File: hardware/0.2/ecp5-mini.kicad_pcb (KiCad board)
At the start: 4 copper layers, 52 x 27 mm, 105 parts, among them J1 Micro_SD_Card, J2 JTAG, J3 S7 Mini, J4 S7 Mini, J5 USB_C_Receptacle_USB2.0, Q1 BSS138, Q2 BSS138, Q3 BSS138, Q4 BSS138, SW1 PTS810, U1 ECP5U_12_CABGA256, U2 TLV75525PDQNR, U3 TLV75518PDQNR, U4 USBLC6-2P6, U5 TLV62569DRLR, U6 W25Q128JVPIQ, U7 S27KS0641, U8 TLV62569DRLR, X1 DSC6101CI2A-016.0000

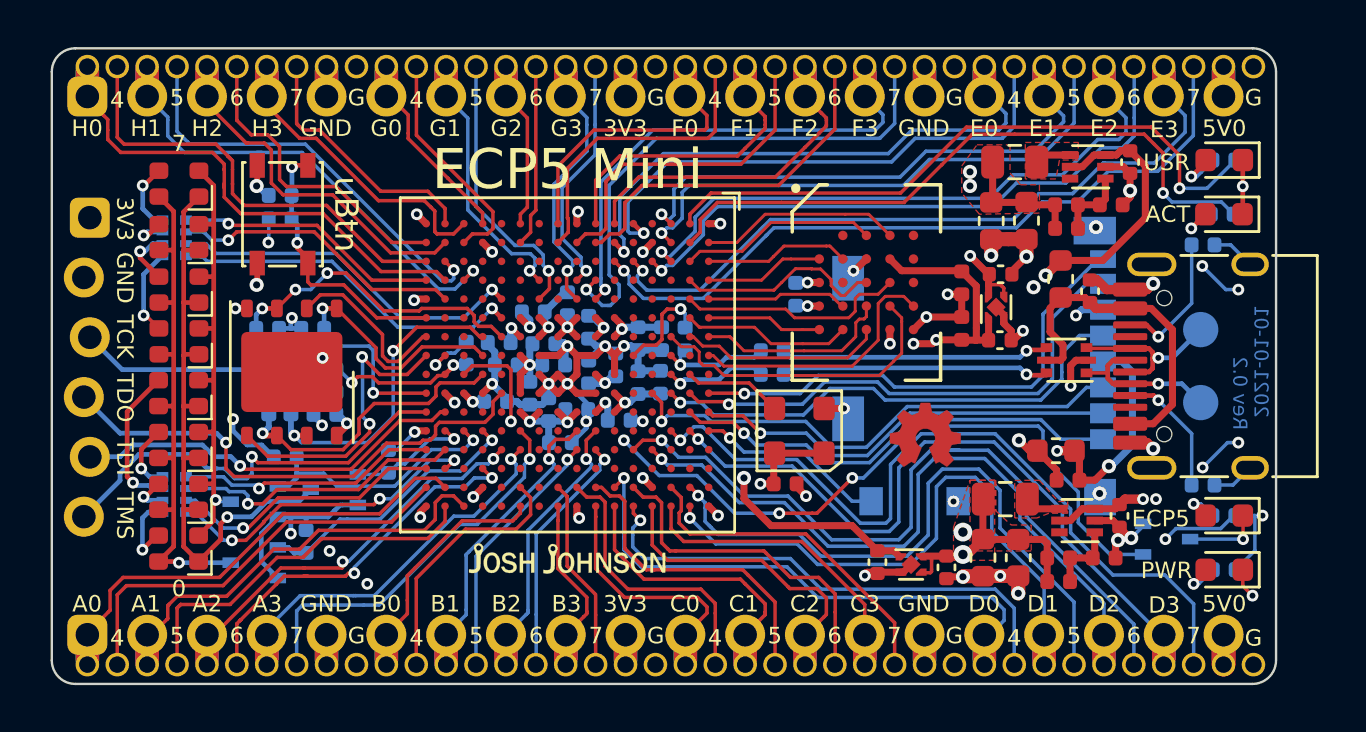
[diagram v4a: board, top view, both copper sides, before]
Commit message: hyperram now length matched
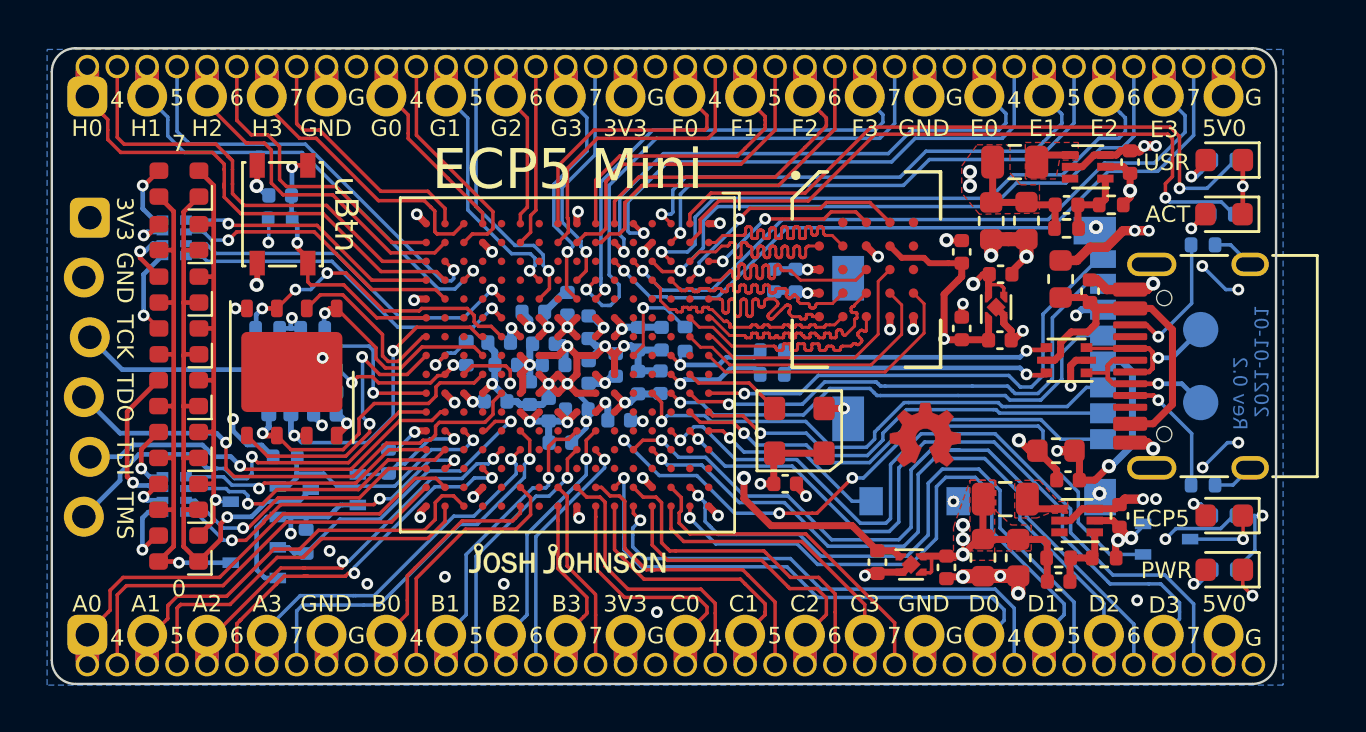
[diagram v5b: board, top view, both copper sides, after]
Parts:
- added C28: 4u7, Capacitor_SMD:C_0402_1005Metric, B.Cu at (126.9, 91.3)
- moved C46 1.32 mm to (134.8, 90.1), turned to 90 degrees
- moved C45 0.59 mm to (127.8, 91.3)
- moved U7 0.55 mm to (130.8, 90.8)
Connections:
- net /FPGA Config/D+ renamed Net-(R10-Pad2)
- net /FPGA Config/D- renamed Net-(R9-Pad1)
- U1 pad A2: /HR_nRST -> /HR_CK_P
- U1 pad A3: /HR_CK -> /HR_nCS
- U1 pad A4: /HR_nCK -> /HR_RWDS
- U1 pad A5: /HR_DQ1 -> /HR_DQ7
- U1 pad A6: /HR_DQ7 -> /HR_DQ0
- U1 pad A7: /HR_DQ0 -> /HR_DQ2
- U1 pad B3: /HR_nCS -> /HR_CK_N
- U1 pad B4: /HR_RWDS -> /HR_nRST
- U1 pad B5: /HR_DQ2 -> (no net)
- U1 pad B6: /HR_DQ6 -> /HR_DQ5
- U1 pad B7: /HR_DQ5 -> /HR_DQ3
- U1 pad C4: (no net) -> /HR_DQ1
- U1 pad C7: /HR_DQ3 -> (no net)
- U1 pad D4: (no net) -> /HR_DQ6
- U7 pad B1: /HR_nCK -> /HR_CK_N
- U7 pad B2: /HR_CK -> /HR_CK_P
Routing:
- net /HR_CK_P: track 0.00 -> 11.0 mm
- net /HR_CK_N: track 0.00 -> 11.0 mm
- net /HR_CK: track 6.19 -> 0.00 mm
- net /HR_DQ7: track 4.90 -> 11.0 mm
- net /HR_DQ1: track 5.99 -> 11.1 mm
- net /HR_nCK: track 5.07 -> 0.00 mm
- net +5V: track 52.8 -> 48.1 mm, vias 4 -> 6
- net /HR_DQ6: track 7.20 -> 10.8 mm
- net /HR_DQ0: track 8.35 -> 11.0 mm
- net /HR_DQ5: track 8.60 -> 11.1 mm
- net /HR_RWDS: track 8.90 -> 11.0 mm
- net /HR_nRST: track 8.57 -> 10.5 mm, vias 0 -> 2
- net /LED_B: track 11.8 -> 13.7 mm
- net /PD37+: track 28.9 -> 30.6 mm
- net +1V8: track 29.2 -> 30.8 mm, vias 5 -> 4
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- added copper zone on B.Cu, net GND

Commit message: almost there
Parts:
- moved C21 0.30 mm to (120.2, 95.2)
- moved R6 0.10 mm to (145.1, 100.1)
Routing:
- net +3V3: track 60.3 -> 63.1 mm, vias 22 -> 24
- net /FPGA Config/CFG_IO0: track 12.7 -> 12.1 mm
- net /FPGA Config/TCK: track 17.2 -> 16.6 mm
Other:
- board text added: "2020-12-31"
- board text removed: "2021-01-01"

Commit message: shipped 0.2
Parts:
- added FID1: Fiducial, Fiducial:Fiducial_0.5mm_Mask1mm, F.Cu at (97.8, 86.5)
- added FID2: Fiducial, Fiducial:Fiducial_0.5mm_Mask1mm, F.Cu at (97.8, 103.5)
- added FID3: Fiducial, Fiducial:Fiducial_0.5mm_Mask1mm, F.Cu at (142.2, 104.9)
- added FID500: Fiducial, Fiducial:Fiducial_0.5mm_Mask1mm, B.Cu at (142.2, 104.9)
- added FID501: Fiducial, Fiducial:Fiducial_0.5mm_Mask1mm, B.Cu at (97.8, 86.5)
- added FID502: Fiducial, Fiducial:Fiducial_0.5mm_Mask1mm, B.Cu at (97.8, 103.5)
- D10: renamed from D12; value PINK -> Pink
- D11: renamed from D2; value PINK -> Pink
- D12: renamed from D1; value PINK -> Pink
- D9: renamed from D3; value PINK -> Pink
- J5: value USB_C_Receptacle_USB2.0 -> USB_Type_C_2.0
- R1: value 360K -> 120K
- R3: renamed from R2; value 82K -> 26K7
- X1: value DSC6101CI2A-016.0000 -> 16MHz
- moved C2 0.27 mm to (131.2, 103.5)
- moved C3 0.07 mm to (134.2, 103.5)
- renumbered C14 to C1, C27 to C10, C10 to C11, C11 to C12, C9 to C13, C8 to C14, C12 to C15, C6 to C16, C1 to C17, C2 to C18, C4 to C2, C46 to C4, C47 to C5, C45 to C500, C28 to C501, C23 to C502, C29 to C503, C19 to C504, C25 to C505, C38 to C506, C21 to C507, C37 to C508, C39 to C509, C20 to C510, C26 to C511, C30 to C512, C41 to C513, C32 to C514, C42 to C515, C17 to C516, C22 to C517, C43 to C518, C40 to C519, C31 to C520, C15 to C521, C18 to C522, C13 to C523, C5 to C6, C16 to C8, C24 to C9, D11 to D1, D10 to D2, D9 to D3, D8 to D4, D7 to D5, D5 to D7, D4 to D8, Q1 to Q500, Q2 to Q501, Q3 to Q502, Q4 to Q503, R3 to R2, R22 to R500, R21 to R501, R5 to R502, R23 to R503, R7 to R504, R6 to R505, R10 to R506, R9 to R507, R11 to R508, R20 to R509, R25 to R510, R19 to R511, R29 to R512, R30 to R513, R24 to R514, R28 to R515, R12 to R516, R8 to R517, R26 to R518, R27 to R519, RN3 to RN500, RN2 to RN501, TP1 to TP500, TP2 to TP501, U6 to U1, U1 to U2, U7 to U3, U2 to U4, U3 to U5, U4 to U6, U5 to U7
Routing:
- net GND: track 98.5 -> 98.9 mm, vias 62 -> 61

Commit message: release v0.2 for real this time
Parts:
- moved C15 3.19 mm to (139.4, 96.6)
- moved C12 0.87 mm to (139.3, 97.8)
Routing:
- net +3V3: track 63.1 -> 58.4 mm
- net /SD_CMD: track 22.1 -> 23.4 mm
- net /SD_DAT2: track 19.5 -> 20.6 mm
- net GND: track 98.9 -> 100.0 mm
- net /PD37-: track 33.5 -> 34.4 mm
- net /SD_DAT3: track 18.6 -> 19.5 mm
- net /FPGA Config/CFG_CDONE: track 37.1 -> 37.8 mm
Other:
- board text added: "2021-01-03"
- board text removed: "2020-12-31"
